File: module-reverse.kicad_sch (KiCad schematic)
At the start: 15 parts, among them J1 Screw_Terminal_01x04, J2 Screw_Terminal_01x04, J3 Screw_Terminal_01x04, J4 Screw_Terminal_01x04, J5 Screw_Terminal_01x04, K1 AZ733-2CE-12DE, U1 MIC2940A-12WT

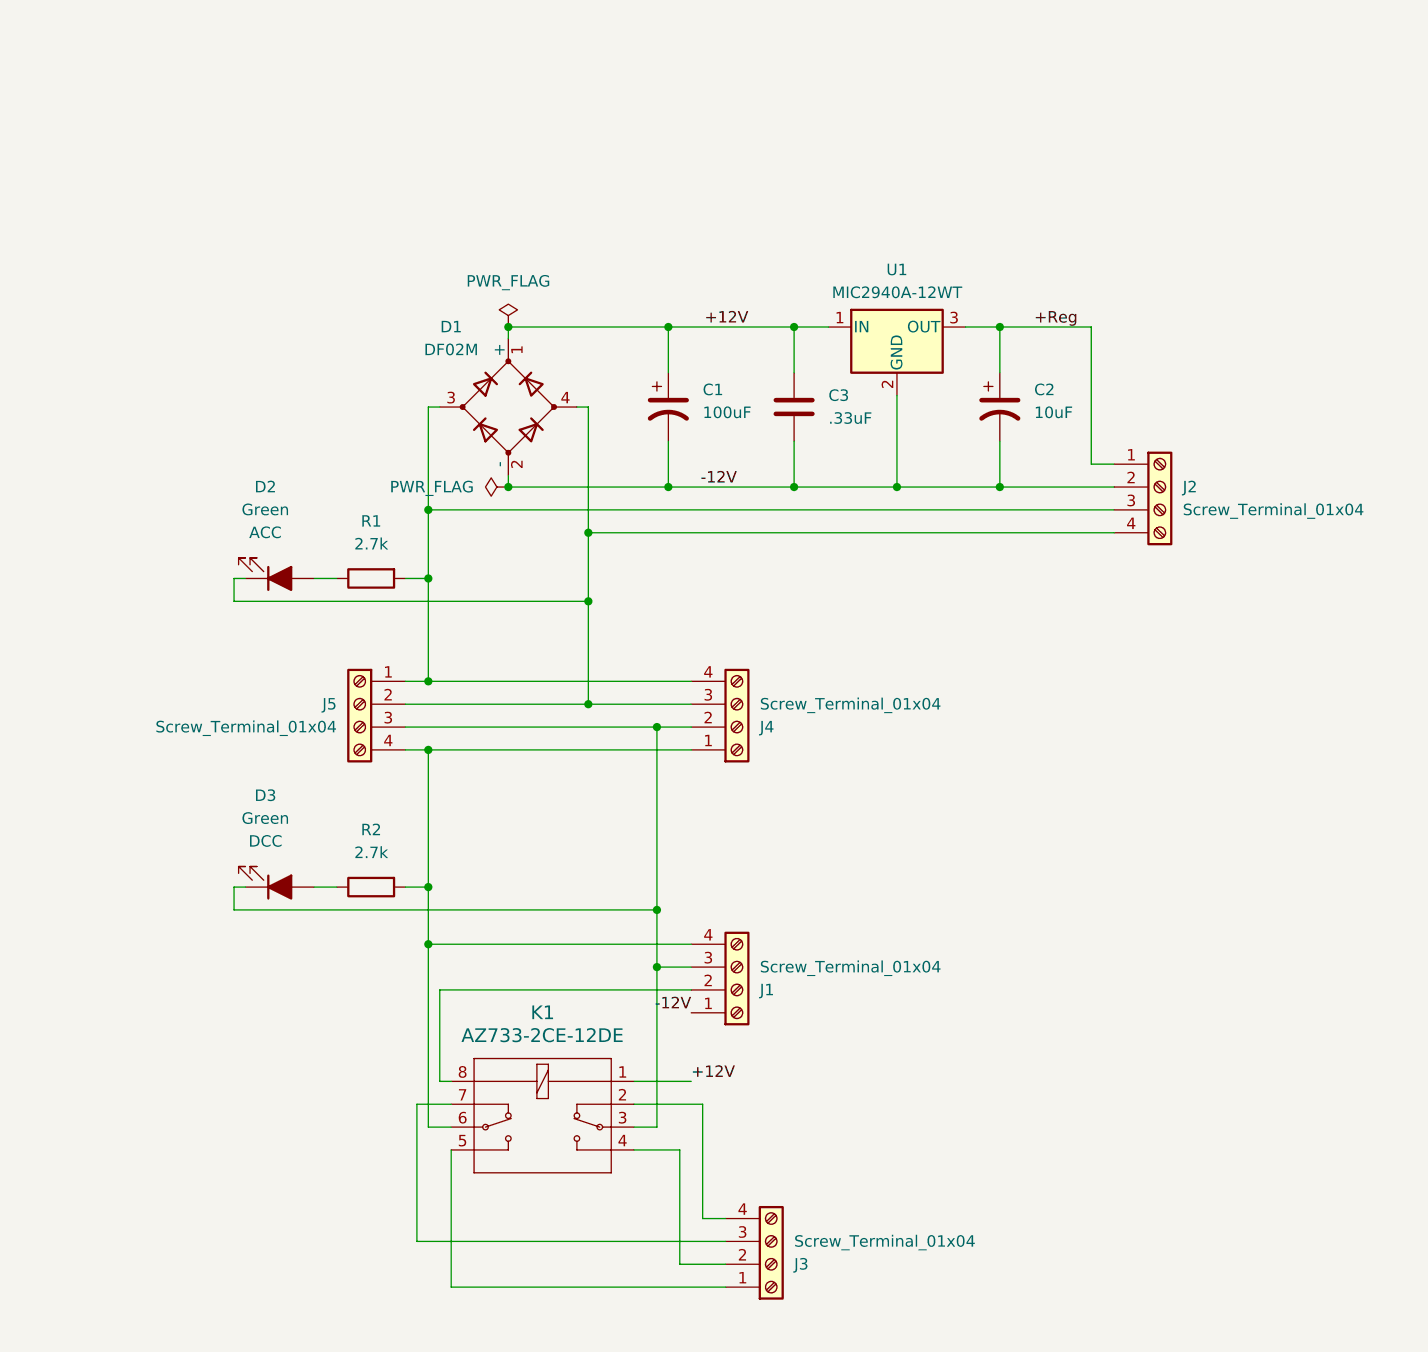
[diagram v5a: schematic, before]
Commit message: Added a PTC fuse to the ACC power and an additional LED to show its status
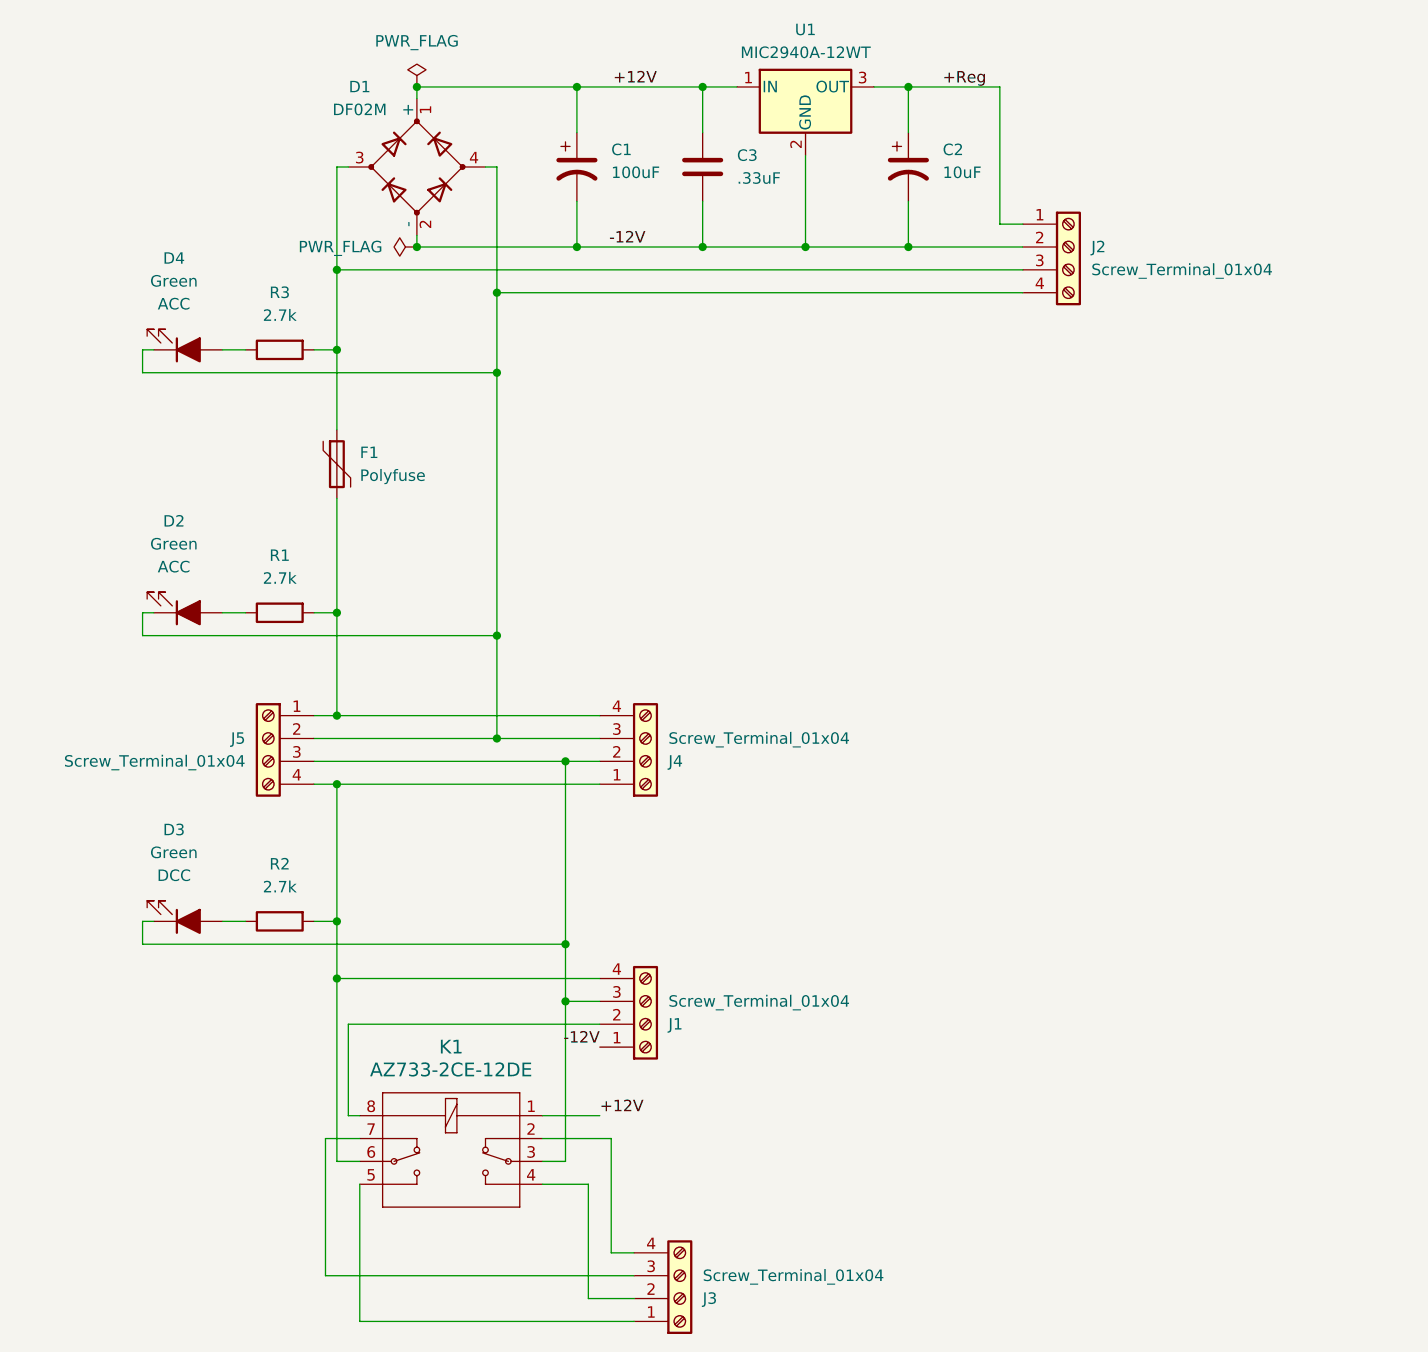
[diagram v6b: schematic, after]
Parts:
- added D4: Green, LED_THT:LED_D3.0mm, symbol Device:LED_Filled
- added F1: Polyfuse, Fuse:Fuse_BelFuse_0ZRE0005FF_L8.3mm_W3.8mm, symbol Device:Polyfuse
- added R3: 2.7k, Resistor_THT:R_Axial_DIN0207_L6.3mm_D2.5mm_P10.16mm_Horizontal, symbol Device:R
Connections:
- net at D1.4, D2.1 (K), J2.4 (Pin_4)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: now also D4.1 (K)
- net at J4.4 (Pin_4), J5.1 (Pin_1), R1.2: now also F1.2; no longer D1.3, J2.3 (Pin_3)
- new net: D4.2 (A), R3.1
- new net: D1.3, F1.1, J2.3 (Pin_3), R3.2
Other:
- moved on the sheet: C1, C2, C3, D1, D2, D3, J1, J2, J3, J4, J5, K1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

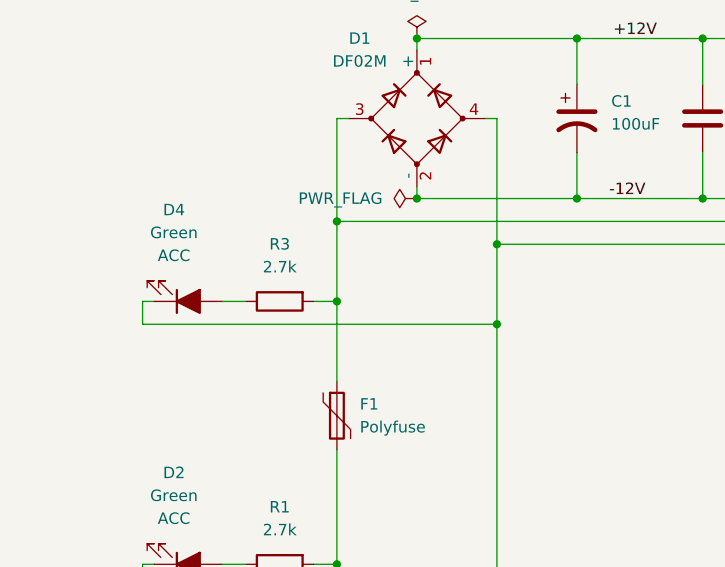
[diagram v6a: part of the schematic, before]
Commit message: Updated LEDs
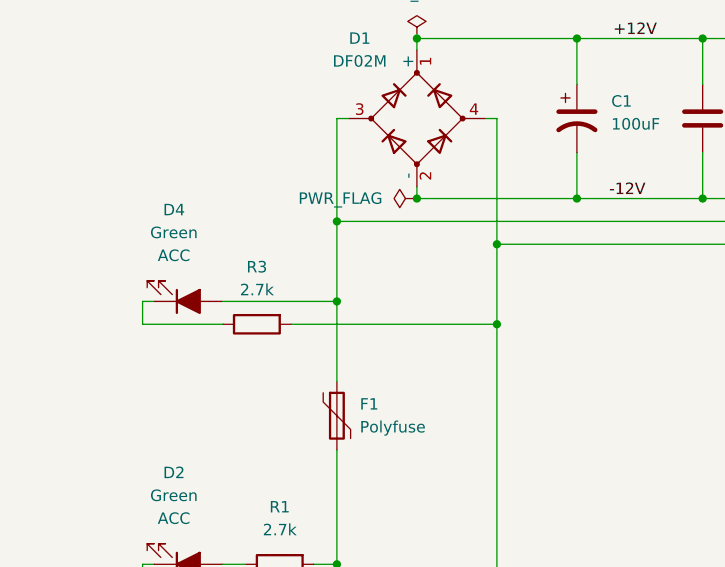
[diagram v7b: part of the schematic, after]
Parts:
- F1: footprint Fuse:Fuse_BelFuse_0ZRE0005FF_L8.3mm_W3.8mm -> Fuse:Fuse_Bourns_MF-RG300; MPN (none) -> MF-R020
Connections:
- net at R3.1: now also D4.1 (K); no longer D4.2 (A)
- net at D1.3, F1.1, J2.3 (Pin_3): now also D4.2 (A); no longer R3.2
- net at D1.4, D2.1 (K), J2.4 (Pin_4)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: now also R3.2; no longer D4.1 (K)
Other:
- moved on the sheet: R3
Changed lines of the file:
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@@
+	(wire
+		(pts
+			(xy 91.44 64.77) (xy 114.3 64.77)
+		)
+		(stroke
+			(width 0)
+			(type default)
+		)
+	)
 	(wire
 		(pts
@@
 	(wire
 		(pts
-			(xy 83.82 62.23) (xy 86.36 62.23)
+			(xy 83.82 62.23) (xy 96.52 62.23)
 		)
 		(stroke
@@
 	(wire
 		(pts
-			(xy 74.93 64.77) (xy 114.3 64.77)
-		)
-		(stroke
-			(width 0)
-			(type default)
-		)
-	)
-	(wire
-		(pts
-			(xy 93.98 62.23) (xy 96.52 62.23)
+			(xy 74.93 64.77) (xy 83.82 64.77)
 		)
 		(stroke
@@
 	(symbol
 		(lib_id "Device:R")
-		(at 90.17 62.23 90)
+		(at 87.63 64.77 90)
 		(mirror x)
 		(unit 1)
@@
 		(dnp no)
 		(property "Reference" "R3"
-			(at 90.17 55.88 90)
+			(at 87.63 58.42 90)
 			(effects
 				(font
@@
 		)
 		(property "Value" "2.7k"
-			(at 90.17 58.42 90)
+			(at 87.63 60.96 90)
 			(effects
 				(font
@@
 		)
 		(property "Footprint" "Resistor_THT:R_Axial_DIN0207_L6.3mm_D2.5mm_P10.16mm_Horizontal"
-			(at 90.17 60.452 90)
+			(at 87.63 62.992 90)
 			(effects
 				(font
@@
 		)
 		(property "Datasheet" "~"
-			(at 90.17 62.23 0)
+			(at 87.63 64.77 0)
 			(effects
 				(font
@@
 		)
 		(property "Description" ""
-			(at 90.17 62.23 0)
+			(at 87.63 64.77 0)
 			(effects
 				(font
@@
 		)
 		(property "MPN" "CFR-25JB-52-2K7"
-			(at 90.17 62.23 0)
+			(at 87.63 64.77 0)
 			(effects
 				(font
@@
 			)
 		)
-		(property "Footprint" "Fuse:Fuse_BelFuse_0ZRE0005FF_L8.3mm_W3.8mm"
+		(property "Footprint" "Fuse:Fuse_Bourns_MF-RG300"
 			(at 97.79 80.01 0)
 			(effects
@@
 			(at 96.52 74.93 0)
 			(effects
+				(font
+					(size 1.27 1.27)
+				)
+				(hide yes)
+			)
+		)
+		(property "MPN" "MF-R020"
+			(at 96.52 74.93 0)
+			(effects
